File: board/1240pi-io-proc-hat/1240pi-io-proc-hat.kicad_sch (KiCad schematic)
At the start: 10 parts, among them J1 62684-50210, J2 SFV10R-1ST, P445 Header, U445 Z80

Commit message: Rotate sockets on hat boards 180 to match actual orientation.
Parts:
- R1, R2, R3, R4, R5, R6: value (none) -> 10k; footprint (none) -> Resistor_SMD:R_0805_2012Metric
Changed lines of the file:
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@@
     (title "1240-Pi I/O Processor Mod")
     (date "2022-05-21")
-    (rev "1.0")
+    (rev "1.1")
     (company "© 2022 Sam Hanes, licensed under CERN-OHL-S v2+")
     (comment 1 "https://github.com/Elemecca/1240pi")
@@
     (in_bom yes) (on_board yes)
     (property "Reference" "R3" (id 0) (at 46.99 182.118 90))
-    (property "Value" "" (id 1) (at 46.99 184.15 90))
-    (property "Footprint" "" (id 2) (at 46.99 185.928 90)
+    (property "Value" "10k" (id 1) (at 46.99 184.15 90))
+    (property "Footprint" "Resistor_SMD:R_0805_2012Metric" (id 2) (at 46.99 185.928 90)
       (effects (font (size 1.27 1.27)) hide)
     )
@@
     (in_bom yes) (on_board yes)
     (property "Reference" "R2" (id 0) (at 46.99 177.038 90))
-    (property "Value" "" (id 1) (at 46.99 179.07 90))
-    (property "Footprint" "" (id 2) (at 46.99 180.848 90)
+    (property "Value" "10k" (id 1) (at 46.99 179.07 90))
+    (property "Footprint" "Resistor_SMD:R_0805_2012Metric" (id 2) (at 46.99 180.848 90)
       (effects (font (size 1.27 1.27)) hide)
     )
@@
     (in_bom yes) (on_board yes)
     (property "Reference" "R6" (id 0) (at 46.99 197.358 90))
-    (property "Value" "" (id 1) (at 46.99 199.39 90))
-    (property "Footprint" "" (id 2) (at 46.99 201.168 90)
+    (property "Value" "10k" (id 1) (at 46.99 199.39 90))
+    (property "Footprint" "Resistor_SMD:R_0805_2012Metric" (id 2) (at 46.99 201.168 90)
       (effects (font (size 1.27 1.27)) hide)
     )
@@
     (in_bom yes) (on_board yes)
     (property "Reference" "R1" (id 0) (at 46.99 171.958 90))
-    (property "Value" "" (id 1) (at 46.99 173.99 90))
-    (property "Footprint" "" (id 2) (at 46.99 175.768 90)
+    (property "Value" "10k" (id 1) (at 46.99 173.99 90))
+    (property "Footprint" "Resistor_SMD:R_0805_2012Metric" (id 2) (at 46.99 175.768 90)
       (effects (font (size 1.27 1.27)) hide)
     )
@@
     (in_bom yes) (on_board yes)
     (property "Reference" "R5" (id 0) (at 46.99 192.278 90))
-    (property "Value" "" (id 1) (at 46.99 194.31 90))
-    (property "Footprint" "" (id 2) (at 46.99 196.088 90)
+    (property "Value" "10k" (id 1) (at 46.99 194.31 90))
+    (property "Footprint" "Resistor_SMD:R_0805_2012Metric" (id 2) (at 46.99 196.088 90)
       (effects (font (size 1.27 1.27)) hide)
     )
@@
     (in_bom yes) (on_board yes)
     (property "Reference" "R4" (id 0) (at 46.99 187.198 90))
-    (property "Value" "" (id 1) (at 46.99 189.23 90))
-    (property "Footprint" "" (id 2) (at 46.99 191.008 90)
-      (effects (font (size 1.27 1.27)) hide)
-    )
+    (property "Value" "10k" (id 1) (at 46.99 189.23 90))
+    (property "Footprint" "Resistor_SMD:R_0805_2012Metric" (id 2) (at 46.99 191.008 90)
+      (effects (font (size 1.27 1.27)) hide)
+    )

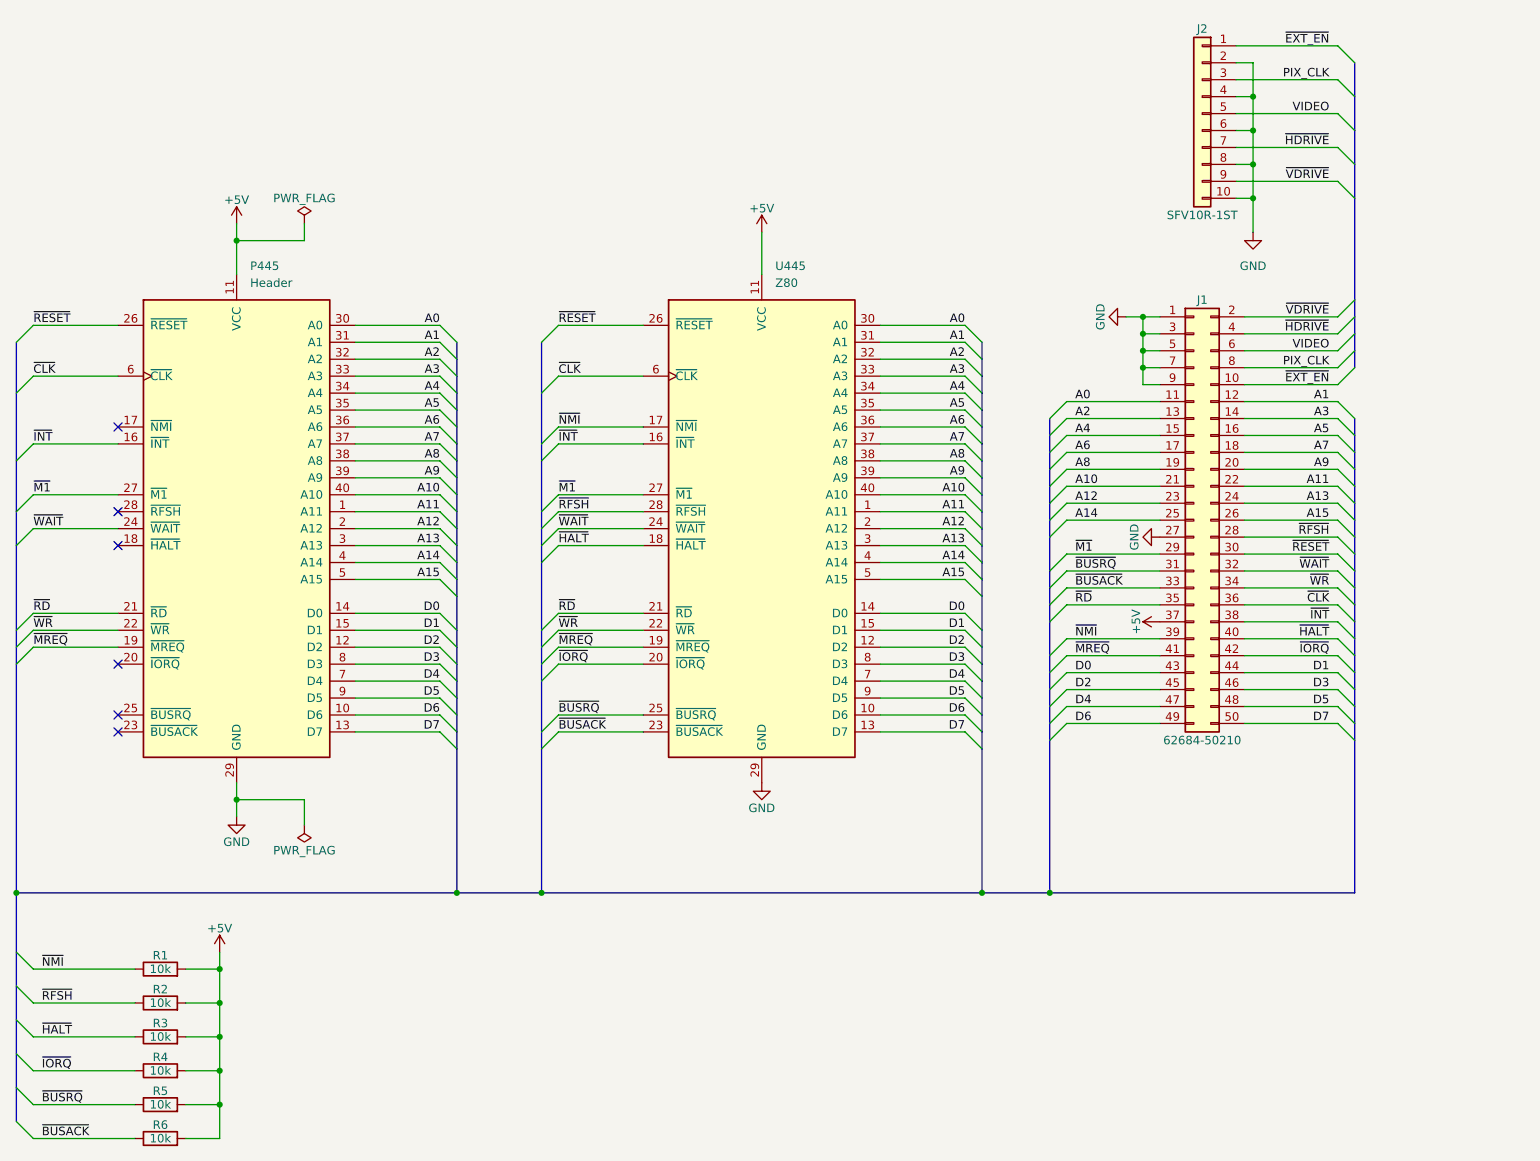
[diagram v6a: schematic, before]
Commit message: Rearrange IO Proc hat, add IO Proc interface.
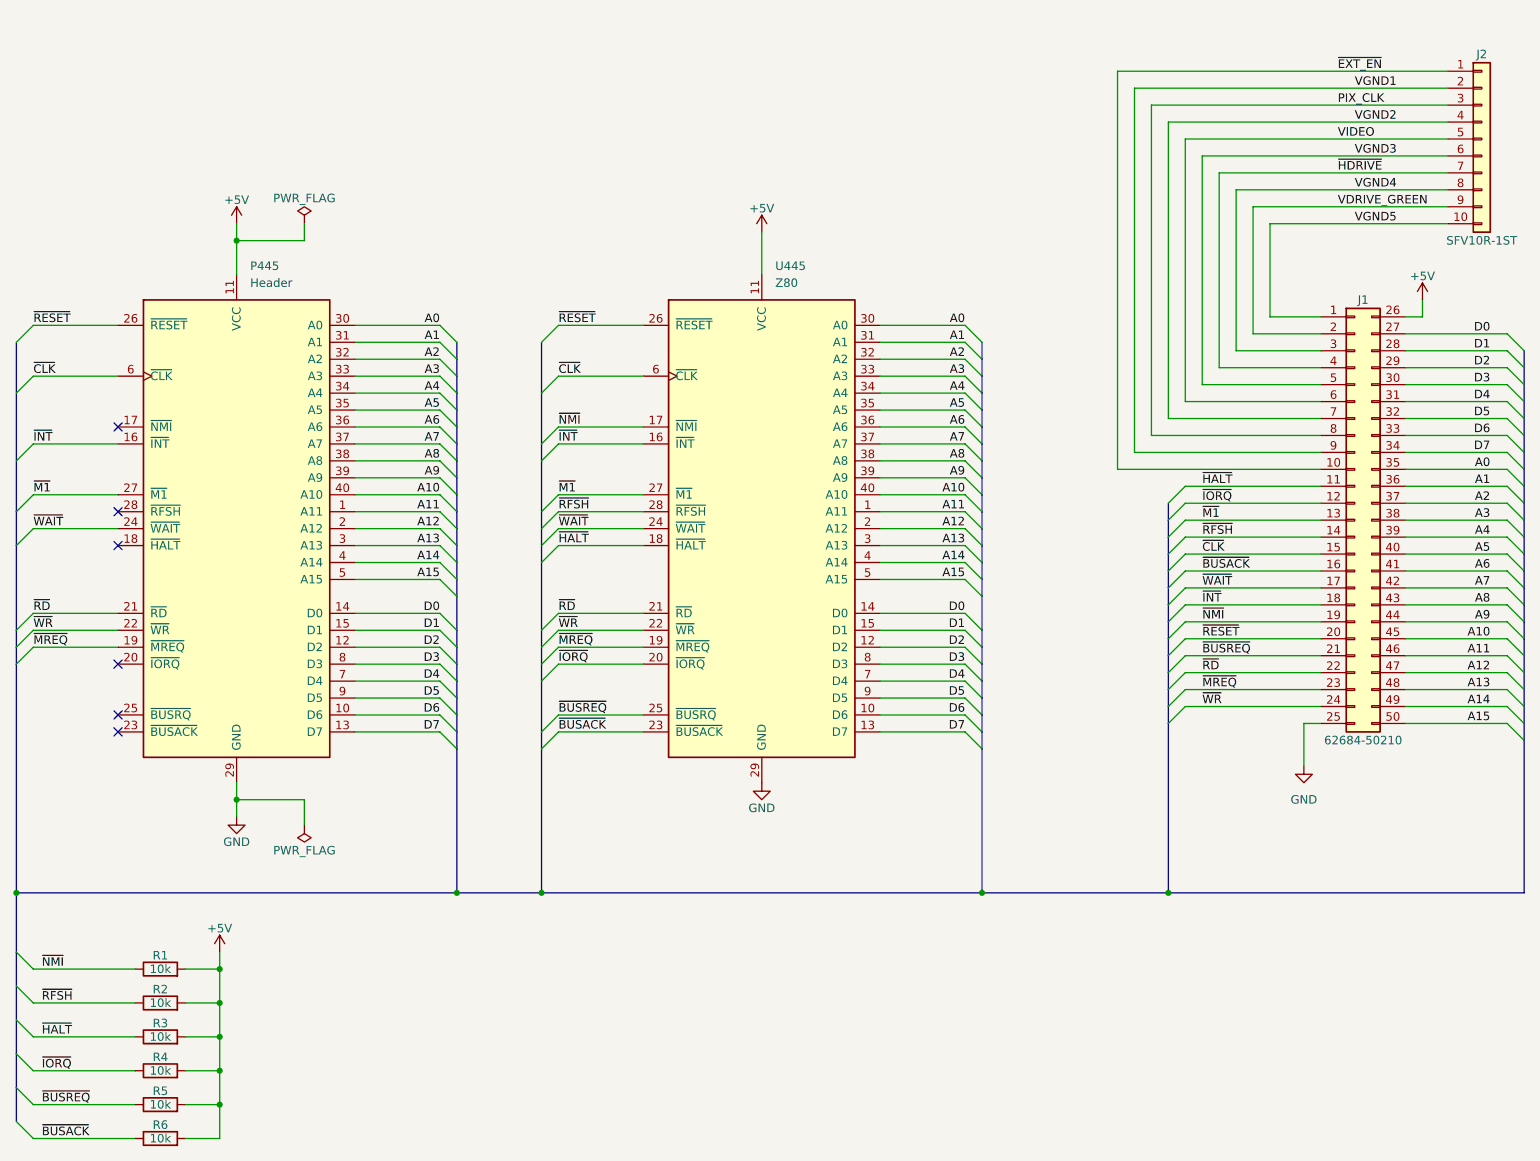
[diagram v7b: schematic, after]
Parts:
- removed J1: 62684-50210, 0Local:Amphenol_62684-50210, symbol Connector_Generic:Conn_02x25_Odd_Even
- added J1: 62684-50210, 0Local:Amphenol_62684-50210, symbol Connector_Generic:Conn_02x25_Top_Bottom
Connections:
- net +5V: now also J1.26 (Pin_26)
- net A0: now also J1.35 (Pin_35)
- net A1: now also J1.36 (Pin_36)
- net A10: now also J1.45 (Pin_45)
- net A11: now also J1.46 (Pin_46)
- net A12: now also J1.47 (Pin_47)
- net A13: now also J1.48 (Pin_48)
- net A14: now also J1.49 (Pin_49)
- net A15: now also J1.50 (Pin_50)
- net A2: now also J1.37 (Pin_37)
- net A3: now also J1.38 (Pin_38)
- net A4: now also J1.39 (Pin_39)
- net A5: now also J1.40 (Pin_40)
- net A6: now also J1.41 (Pin_41)
- net A7: now also J1.42 (Pin_42)
- net A8: now also J1.43 (Pin_43)
- net A9: now also J1.44 (Pin_44)
- net D0: now also J1.27 (Pin_27)
- net D1: now also J1.28 (Pin_28)
- net D2: now also J1.29 (Pin_29)
- net D3: now also J1.30 (Pin_30)
- net D4: now also J1.31 (Pin_31)
- net D5: now also J1.32 (Pin_32)
- net D6: now also J1.33 (Pin_33)
- net D7: now also J1.34 (Pin_34)
- net GND: now also J1.25 (Pin_25); no longer J2.10 (Pin_10), J2.2 (Pin_2), J2.4 (Pin_4), J2.6 (Pin_6), J2.8 (Pin_8)
- net PIX_CLK: now also J1.8 (Pin_8)
- net VIDEO: now also J1.6 (Pin_6)
- net ~{BUSACK}: now also J1.16 (Pin_16)
- net ~{CLK}: now also J1.15 (Pin_15)
- net ~{EXT_EN}: now also J1.10 (Pin_10)
- net ~{HALT}: now also J1.11 (Pin_11)
- net ~{HDRIVE}: now also J1.4 (Pin_4)
- net ~{INT}: now also J1.18 (Pin_18)
- net ~{IORQ}: now also J1.12 (Pin_12)
- net ~{M1}: now also J1.13 (Pin_13)
- net ~{MREQ}: now also J1.23 (Pin_23)
- net ~{NMI}: now also J1.19 (Pin_19)
- net ~{RD}: now also J1.22 (Pin_22)
- net ~{RESET}: now also J1.20 (Pin_20)
- net ~{RFSH}: now also J1.14 (Pin_14)
- net ~{WAIT}: now also J1.17 (Pin_17)
- net ~{WR}: now also J1.24 (Pin_24)
- net ~{BUSRQ} renamed ~{BUSREQ}
- net ~{BUSREQ}: now also J1.21 (Pin_21)
- net ~{VDRIVE} renamed VDRIVE_GREEN
- net VDRIVE_GREEN: now also J1.2 (Pin_2)
- new net VGND1: J1.9 (Pin_9), J2.2 (Pin_2)
- new net VGND2: J1.7 (Pin_7), J2.4 (Pin_4)
- new net VGND3: J1.5 (Pin_5), J2.6 (Pin_6)
- new net VGND4: J1.3 (Pin_3), J2.8 (Pin_8)
- new net VGND5: J1.1 (Pin_1), J2.10 (Pin_10)
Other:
- moved on the sheet: J2

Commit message: Add description to IO proc interface.
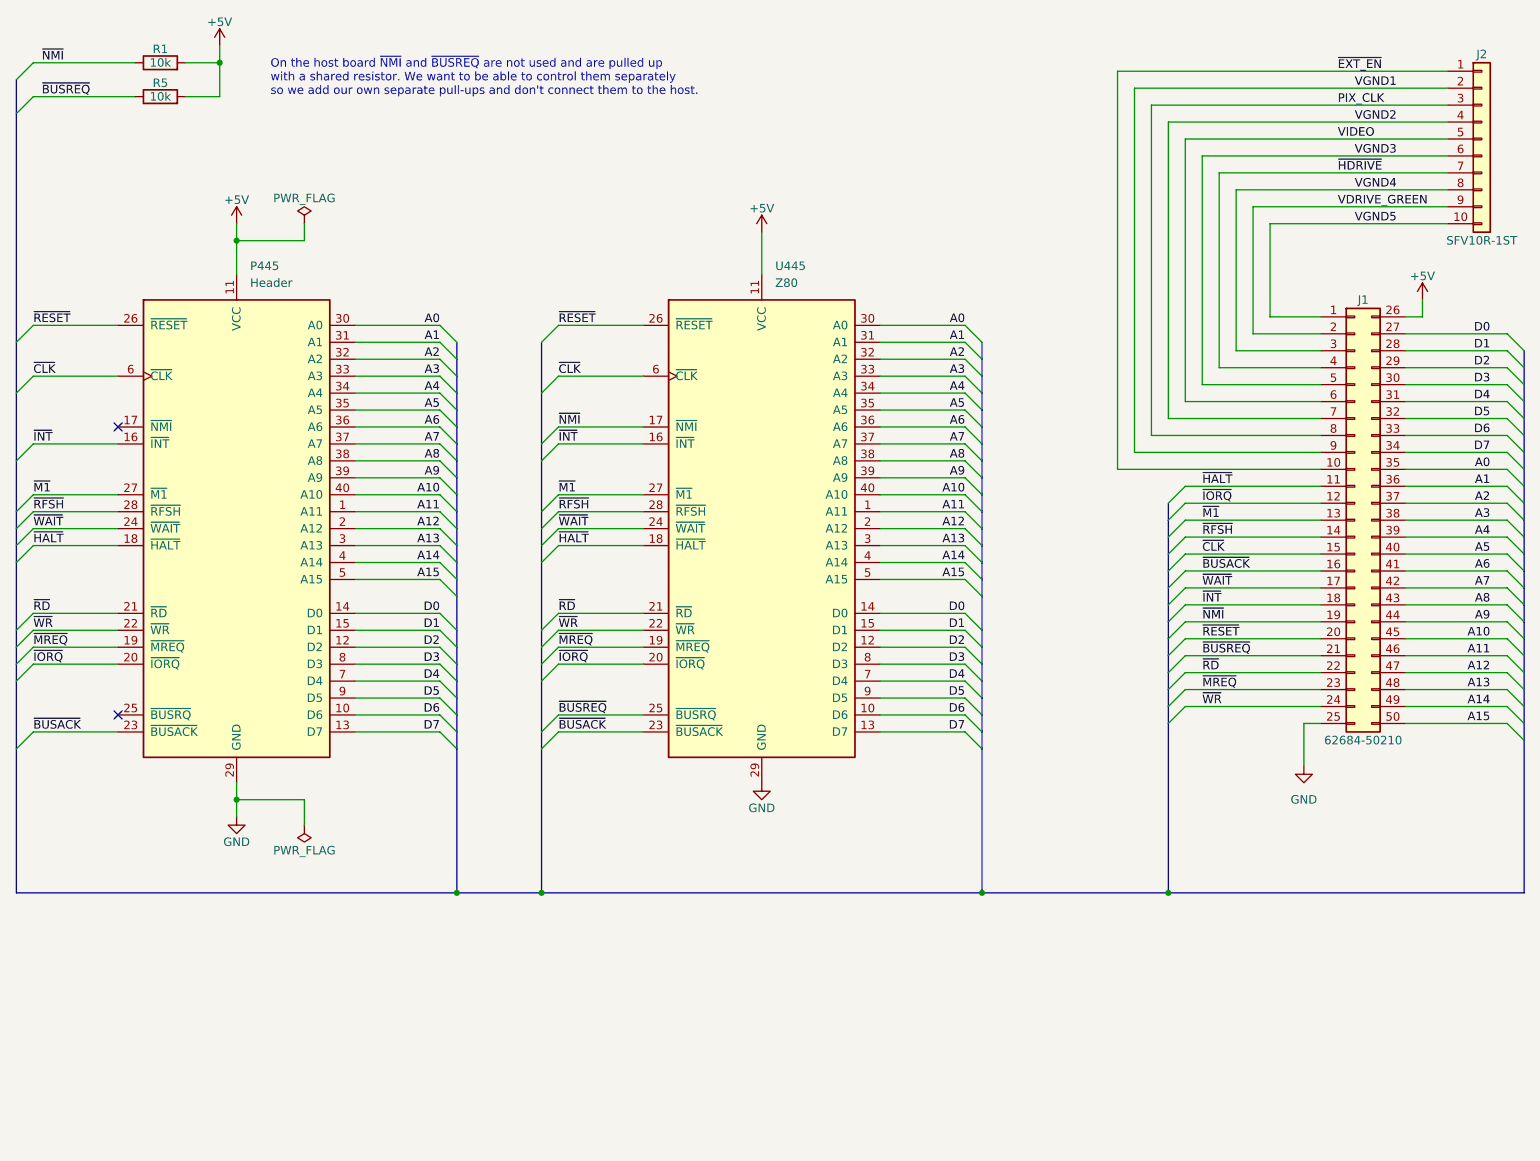
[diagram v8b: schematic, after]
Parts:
- removed R2, R3, R4, R6: 10k, Resistor_SMD:R_0805_2012Metric, symbol Device:R
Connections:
- net ~{BUSACK}: now also P445.23 (~{BUSACK})
- net ~{HALT}: now also P445.18 (~{HALT})
- net ~{IORQ}: now also P445.20 (~{IORQ})
- net ~{RFSH}: now also P445.28 (~{RFSH})
- no-connect marks 6 -> 2
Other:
- note added: "On the host board ~{NMI} and ~{BUSREQ} are not used and are pulled up with a shared resistor. We want to be able to control them separately so we add our own separate pull-ups and don't connect them to the host."
- moved on the sheet: R1, R5
